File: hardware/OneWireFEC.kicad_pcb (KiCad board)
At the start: 2 copper layers, 24 x 27.9 mm, 26 parts, among them J1 105444-0001, J2 B2B-XH-A, U1 PIC16F1454, U2 DS2482S, U3 MIC2091

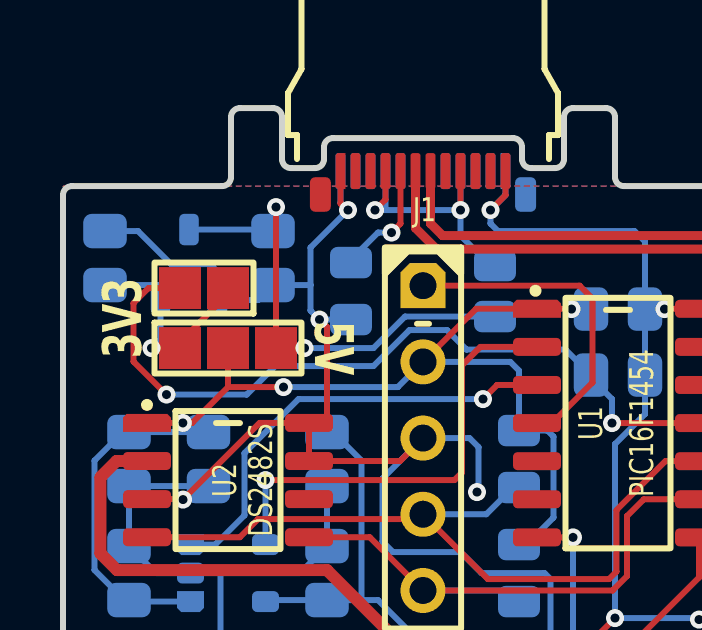
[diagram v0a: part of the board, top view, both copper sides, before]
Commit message: Adjusting solder-on jumpers to be more symetric
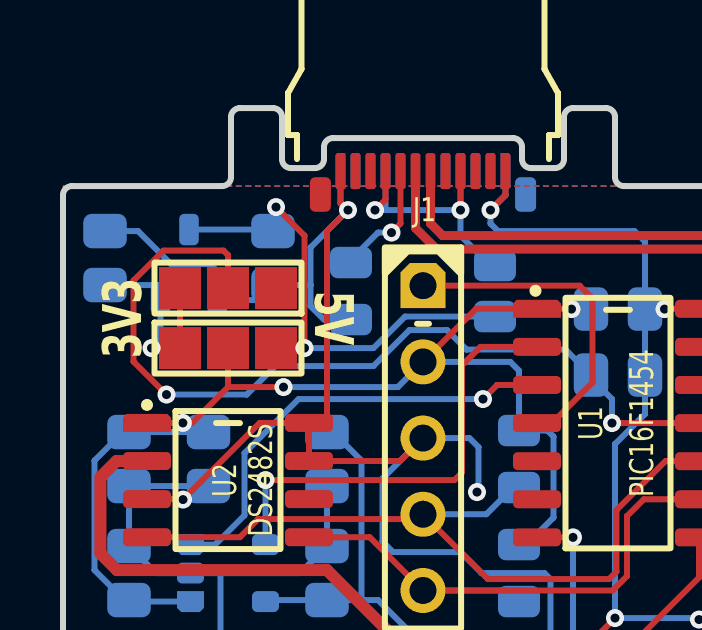
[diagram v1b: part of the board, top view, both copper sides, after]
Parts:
- JP2: footprint Medo64:JP (0805) -> Medo64:JP Dual (1205)
- moved JP2 0.80 mm to (25.5, 26.0)
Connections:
- JP2 pad 1: 3V3 -> (no net)
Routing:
- net GND: track 126.4 -> 130.1 mm, vias 10 -> 9
- net 3V3_USB: track 25.5 -> 29.2 mm
- net 5V: track 15.9 -> 17.2 mm
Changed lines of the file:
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@@
 		)
 	)
-	(footprint "Medo64:JP (0805)"
+	(footprint "Medo64:JP Dual (1205)"
 		(layer "F.Cu")
-		(at 24.7 26 180)
+		(at 25.5 26 180)
 		(property "Reference" "JP2"
-			(at 0 -1.5 0)
+			(at 0 -1.5 180)
 			(layer "F.SilkS")
 			(hide yes)
@@
 		)
 		(property "Value" "Jumper"
-			(at 0 1.6 0)
+			(at 0 1.6 180)
 			(layer "F.SilkS")
 			(hide yes)
@@
 			)
 		)
-		(property "Footprint" "Medo64:JP (0805)"
+		(property "Footprint" "Medo64:JP Dual (1205)"
 			(at 0 0 180)
 			(unlocked yes)
@@
 		(attr smd)
 		(fp_rect
-			(start -1.65 -0.85)
-			(end 1.65 0.85)
+			(start -2.45 -0.85)
+			(end 2.45 0.85)
 			(stroke
 				(width 0.2)
@@
 		)
 		(fp_rect
-			(start -0.1 -0.7)
-			(end 0.1 0.7)
+			(start 0.9 -0.7)
+			(end 0.7 0.7)
+			(stroke
+				(width 0)
+				(type solid)
+			)
+			(fill solid)
+			(layer "F.Mask")
+		)
+		(fp_rect
+			(start -0.9 -0.7)
+			(end -0.7 0.7)
 			(stroke
 				(width 0)
@@
 		)
 		(fp_rect
-			(start -1.75 -0.95)
-			(end 1.75 0.95)
+			(start -2.55 -0.95)
+			(end 2.55 0.95)
 			(stroke
 				(width 0.01)
@@
 		)
 		(pad "1" smd roundrect
-			(at -0.8 0 180)
+			(at -1.6 0 180)
 			(size 1.4 1.4)
 			(layers "F.Cu" "F.Mask")
@@
 			(chamfer_ratio 0)
 			(chamfer top_right bottom_right)
-			(net 13 "3V3")
 			(thermal_bridge_angle 45)
 		)
 		(pad "2" smd roundrect
-			(at 0.8 0 180)
+			(at 0 0 180)
+			(size 1.4 1.4)
+			(layers "F.Cu" "F.Mask")
+			(roundrect_rratio 0)
+			(chamfer_ratio 0)
+			(chamfer top_left top_right bottom_left bottom_right)
+			(net 20 "3V3_USB")
+			(thermal_bridge_angle 45)
+		)
+		(pad "3" smd roundrect
+			(at 1.6 0 180)
 			(size 1.4 1.4)
 			(layers "F.Cu" "F.Mask")
@@
 			(chamfer_ratio 0)
 			(chamfer top_left bottom_left)
-			(net 20 "3V3_USB")
+			(net 13 "3V3")
 			(thermal_bridge_angle 45)
 		)
@@
 	)
 	(gr_text "5V"
-		(at 29 28 270)
+		(at 29 27 270)
 		(layer "F.SilkS" knockout)
 		(effects
@@
 	)
 	(segment
-		(start 28.55 27.05)
-		(end 28.8 27.3)
-		(width 0.2)
-		(layer "F.Cu")
-		(net 4)
-	)
-	(segment
 		(start 29.25 23.182417)
 		(end 29.428008 23.360425)
@@
 	)
 	(segment
+		(start 28.8 30.245)
+		(end 28.8 24.1)
+		(width 0.2)
+		(layer "F.Cu")
+		(net 4)
+	)
+	(segment
 		(start 34.75 22.1)
 		(end 34.75 22.9)
@@
 	)
 	(segment
-		(start 29.25 22.1)
-		(end 29.25 23.182417)
+		(start 28.55 30.495)
+		(end 28.8 30.245)
 		(width 0.2)
 		(layer "F.Cu")
@@
 	)
 	(segment
-		(start 28.8 30.245)
-		(end 28.55 30.495)
+		(start 29.25 22.1)
+		(end 29.25 23.182417)
 		(width 0.2)
 		(layer "F.Cu")
@@
 	)
 	(segment
-		(start 28.8 27.3)
-		(end 28.8 30.245)
+		(start 28.8 24.1)
+		(end 29.5 23.4)
 		(width 0.2)
 		(layer "F.Cu")
@@
 	)
 	(via
-		(at 28.55 27.05)
-		(size 0.6)
-		(drill 0.3)
-		(layers "F.Cu" "B.Cu")
-		(net 4)
-	)
-	(via
 		(at 33.8 32.8)
 		(size 0.6)
@@
 	)
 	(segment
+		(start 29.6 27.05)
+		(end 28.7 27.05)
+		(width 0.2)
+		(layer "B.Cu")
+		(net 4)
+	)
+	(segment
 		(start 27 25.9)
 		(end 28.25 25.9)
@@
 	)
 	(segment
-		(start 28.25 26.75)
-		(end 28.55 27.05)
-		(width 0.2)
-		(layer "B.Cu")
-		(net 4)
-	)
-	(segment
 		(start 39.2 42.5)
 		(end 38.7 42)
@@
 	)
 	(segment
+		(start 28.25 25.9)
+		(end 28.25 26.6)
+		(width 0.2)
+		(layer "B.Cu")
+		(net 4)
+	)
+	(segment
 		(start 39.4 28.9)
 		(end 39.4 26.7)
@@
 	)
 	(segment
+		(start 28.25 26.6)
+		(end 28.7 27.05)
+		(width 0.2)
+		(layer "B.Cu")
+		(net 4)
+	)
+	(segment
 		(start 40.050002 26.7)
 		(end 39.4 26.7)
@@
 	)
 	(segment
-		(start 28.25 25.9)
-		(end 28.25 26.75)
-		(width 0.2)
-		(layer "B.Cu")
-		(net 4)
-	)
-	(segment
 		(start 23.6 25.2)
 		(end 24.9 25.2)
@@
 	)
 	(segment
-		(start 29.6 27.05)
-		(end 28.55 27.05)
-		(width 0.2)
-		(layer "B.Cu")
-		(net 4)
-	)
-	(segment
 		(start 22.5 24.1)
 		(end 23.6 25.2)
@@
 	(segment
 		(start 27.1 28)
-		(end 27.1 23.3)
+		(end 28 28)
 		(width 0.2)
 		(layer "F.Cu")
@@
 	)
 	(segment
-		(start 27.1 28)
-		(end 28 28)
+		(start 28.05 28)
+		(end 28.05 24.25)
 		(width 0.2)
 		(layer "F.Cu")
@@
 		(net 5)
 	)
+	(segment
+		(start 28.05 24.25)
+		(end 27.1 23.3)
+		(width 0.2)
+		(layer "F.Cu")
+		(net 5)
+	)
+	(segment
+		(start 27.1 28)
+		(end 28.05 28)
+		(width 0.2)
+		(layer "F.Cu")
+		(net 5)
+	)
 	(via
 		(at 28.05 28)
@@
 	(segment
 		(start 23.9 27.8)
-		(end 25.5 26.2)
+		(end 23.9 26)
 		(width 0.2)
 		(layer "F.Cu")
@@
 	)
 	(segment
-		(start 22.85 26)
-		(end 22.35 26.5)
+		(start 25.35 24.75)
+		(end 25.5 24.9)
 		(width 0.2)
 		(layer "F.Cu")
@@
 	(segment
 		(start 22.35 28.45)
-		(end 23.45 29.55)
+		(end 22.35 25.75)
 		(width 0.2)
 		(layer "F.Cu")
@@
 	)
 	(segment
-		(start 22.35 26.5)
+		(start 23.45 29.55)
 		(end 22.35 28.45)
 		(width 0.2)
@@
 	)
 	(segment
-		(start 23.9 26)
-		(end 22.85 26)
+		(start 25.5 24.9)
+		(end 25.5 26)
+		(width 0.2)
+		(layer "F.Cu")
+		(net 20)
+	)
+	(segment
+		(start 23.35 24.75)
+		(end 25.35 24.75)
 		(width 0.2)
 		(layer "F.Cu")
@@
 		(width 0.2)
 		(layer "F.Cu")
+		(net 20)
+	)
+	(segment
+		(start 22.35 25.75)
+		(end 23.35 24.75)
+		(width 0.2)
+		(layer "F.Cu")
